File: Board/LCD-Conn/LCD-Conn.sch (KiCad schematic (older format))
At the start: 2 parts

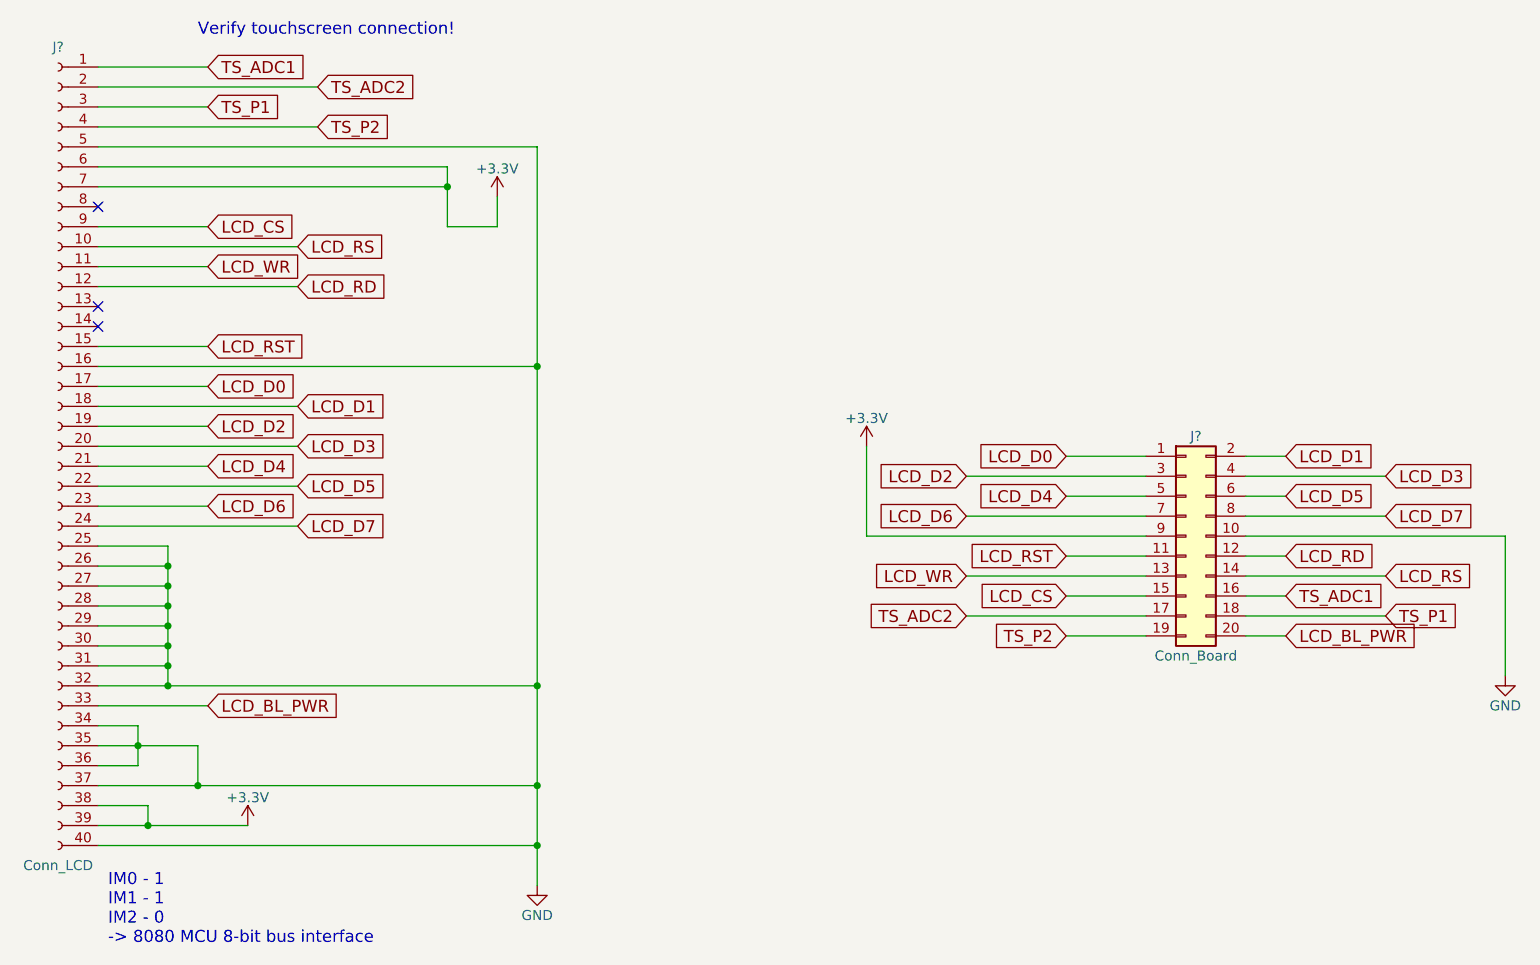
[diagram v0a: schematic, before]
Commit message: system board polished, lcd flex connector footprint updated.
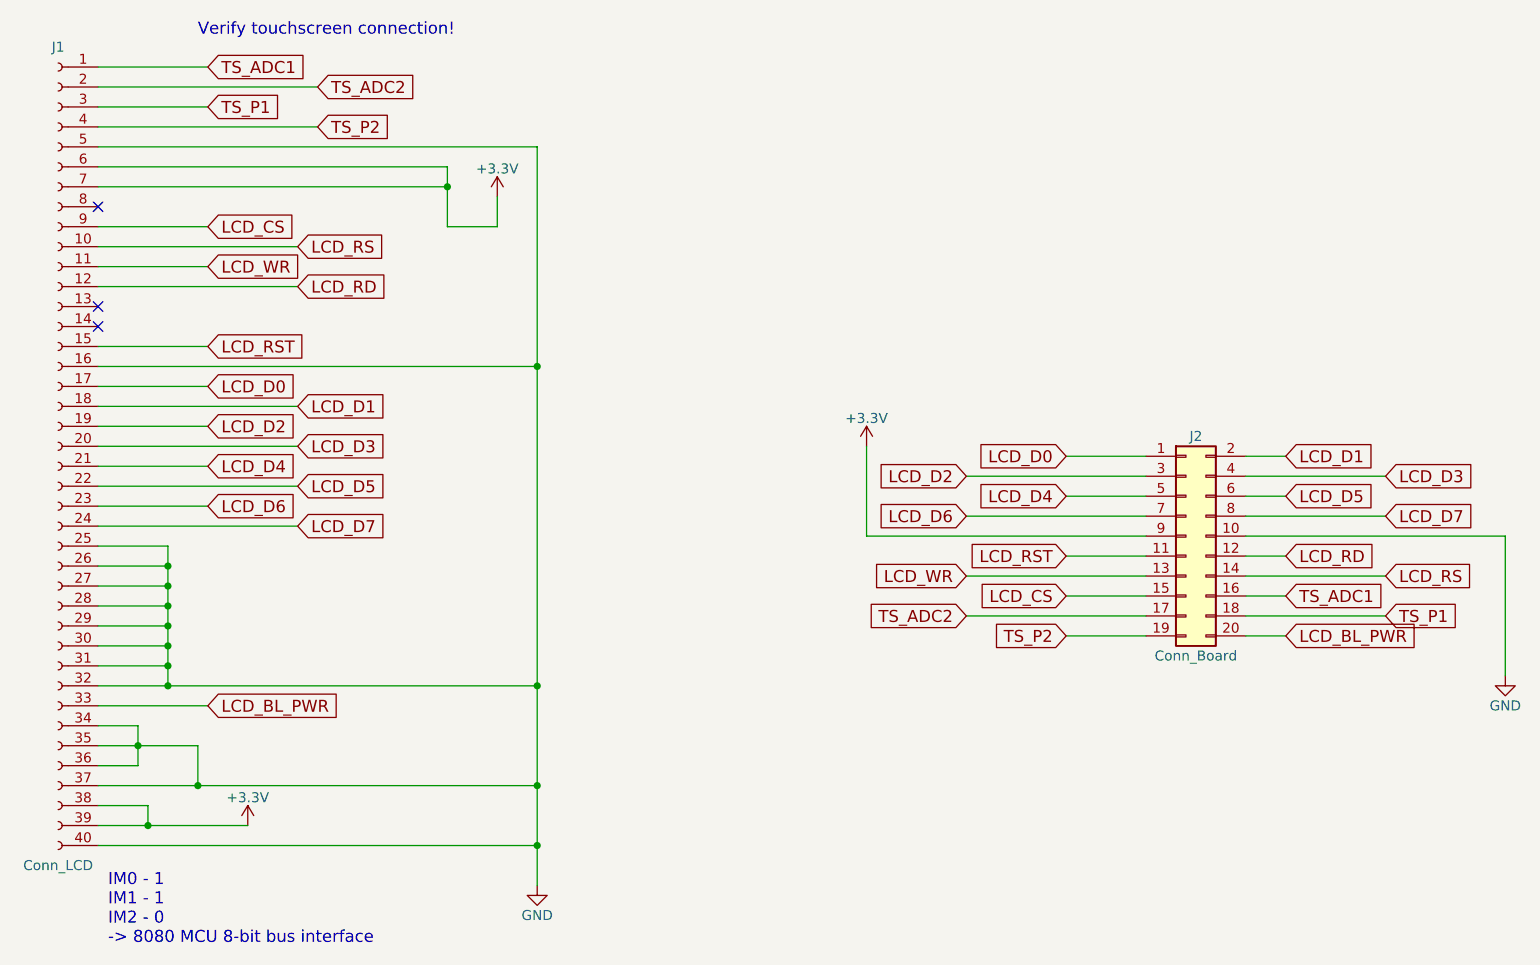
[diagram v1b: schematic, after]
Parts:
- J1: renamed from J?; footprint (none) -> timekiller-footprints:LCD_conn
- J2: renamed from J?; footprint (none) -> Pin_Headers:Pin_Header_Straight_2x10_Pitch2.00mm
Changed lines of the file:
@@
 $EndDescr
 $Comp
-L Conn_01x40_Female J?
+L Conn_01x40_Female J1
 U 1 1 5B8B002C
 P 2450 3700
-F 0 "J?" H 2450 5700 50  0000 C CNN
+F 0 "J1" H 2450 5700 50  0000 C CNN
 F 1 "Conn_LCD" H 2450 1600 50  0000 C CNN
-F 2 "" H 2450 3700 50  0001 C CNN
+F 2 "timekiller-footprints:LCD_conn" H 2450 3700 50  0001 C CNN
 F 3 "" H 2450 3700 50  0001 C CNN
 	1    2450 3700
@@
 $EndComp
 $Comp
-L Conn_02x10_Odd_Even J?
+L Conn_02x10_Odd_Even J2
 U 1 1 5B8B0131
 P 8100 4150
-F 0 "J?" H 8150 4650 50  0000 C CNN
+F 0 "J2" H 8150 4650 50  0000 C CNN
 F 1 "Conn_Board" H 8150 3550 50  0000 C CNN
-F 2 "" H 8100 4150 50  0001 C CNN
+F 2 "Pin_Headers:Pin_Header_Straight_2x10_Pitch2.00mm" H 8100 4150 50  0001 C CNN
 F 3 "" H 8100 4150 50  0001 C CNN
 	1    8100 4150
@@
 	8400 4050 9100 4050
 $Comp
-L +3.3V #PWR?
+L +3.3V #PWR01
 U 1 1 5B8B030D
 P 6500 3700
-F 0 "#PWR?" H 6500 3550 50  0001 C CNN
+F 0 "#PWR01" H 6500 3550 50  0001 C CNN
 F 1 "+3.3V" H 6500 3840 50  0000 C CNN
 F 2 "" H 6500 3700 50  0001 C CNN
@@
 	6500 4150 7900 4150
 $Comp
-L GND #PWR?
+L GND #PWR02
 U 1 1 5B8B0331
 P 9700 4850
-F 0 "#PWR?" H 9700 4600 50  0001 C CNN
+F 0 "#PWR02" H 9700 4600 50  0001 C CNN
 F 1 "GND" H 9700 4700 50  0000 C CNN
 F 2 "" H 9700 4850 50  0001 C CNN
@@
 	2650 2100 3750 2100
 $Comp
-L GND #PWR?
+L GND #PWR03
 U 1 1 5B8B06F6
 P 4850 5900
-F 0 "#PWR?" H 4850 5650 50  0001 C CNN
+F 0 "#PWR03" H 4850 5650 50  0001 C CNN
 F 1 "GND" H 4850 5750 50  0000 C CNN
 F 2 "" H 4850 5900 50  0001 C CNN
@@
 	2650 2200 4850 2200
 Wire Wire Line
-	4850 2200 4850 3300
-Wire Wire Line
-	4850 3300 4850 4900
-Wire Wire Line
-	4850 4900 4850 5400
-Wire Wire Line
-	4850 5400 4850 5700
-Wire Wire Line
-	4850 5700 4850 5900
-$Comp
-L +3.3V #PWR?
+	4850 2200 4850 5900
+$Comp
+L +3.3V #PWR04
 U 1 1 5B8B0735
 P 4650 2450
-F 0 "#PWR?" H 4650 2300 50  0001 C CNN
+F 0 "#PWR04" H 4650 2300 50  0001 C CNN
 F 1 "+3.3V" H 4650 2590 50  0000 C CNN
 F 2 "" H 4650 2450 50  0001 C CNN
@@
 	2650 2300 4400 2300
 Wire Wire Line
-	4400 2300 4400 2400
-Wire Wire Line
-	4400 2400 4400 2600
+	4400 2300 4400 2600
 Wire Wire Line
 	4400 2600 4650 2600
@@
 	2650 4100 3650 4100
 Wire Wire Line
-	2650 4900 3000 4900
-Wire Wire Line
-	3000 4900 4850 4900
-Wire Wire Line
-	3000 4900 3000 4800
-Wire Wire Line
-	3000 4800 3000 4700
-Wire Wire Line
-	3000 4700 3000 4600
-Wire Wire Line
-	3000 4600 3000 4500
-Wire Wire Line
-	3000 4500 3000 4400
-Wire Wire Line
-	3000 4400 3000 4300
-Wire Wire Line
-	3000 4300 3000 4200
+	2650 4900 4850 4900
+Wire Wire Line
+	3000 4200 3000 4900
 Wire Wire Line
 	3000 4200 2650 4200
@@
 Connection ~ 3000 4900
 Wire Wire Line
-	2650 5400 3150 5400
-Wire Wire Line
-	3150 5400 4850 5400
+	2650 5400 4850 5400
 Connection ~ 4850 5400
 Wire Wire Line
 	2650 5100 2850 5100
 Wire Wire Line
-	2850 5100 2850 5200
-Wire Wire Line
-	2850 5200 2850 5300
+	2850 5100 2850 5300
 Wire Wire Line
 	2850 5300 2650 5300
 Wire Wire Line
-	2650 5200 2850 5200
-Wire Wire Line
-	2850 5200 3150 5200
+	2650 5200 3150 5200
 Connection ~ 2850 5200
 Text GLabel 3200 5000 2    60   Input ~ 0
@@
 Connection ~ 4850 5700
 $Comp
-L +3.3V #PWR?
+L +3.3V #PWR05
 U 1 1 5B8B0EE9
 P 3400 5600
-F 0 "#PWR?" H 3400 5450 50  0001 C CNN
+F 0 "#PWR05" H 3400 5450 50  0001 C CNN
 F 1 "+3.3V" H 3400 5740 50  0000 C CNN
 F 2 "" H 3400 5600 50  0001 C CNN
@@
 	2900 5500 2900 5600
 Wire Wire Line
-	2650 5600 2900 5600
-Wire Wire Line
-	2900 5600 3400 5600
+	2650 5600 3400 5600
 Connection ~ 2900 5600
 Text Notes 3150 1650 0    60   ~ 0
